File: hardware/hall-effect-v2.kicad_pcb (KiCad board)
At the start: 2 copper layers, 15 x 25 mm, 24 parts, among them P1 CON-SENSOR2, P2 DEBUG, P3 BOOT, U1 XMC1XXX24, U2 DRV023, U3 DRILL, U4 DRILL, U5 DRILL, U6 DRILL

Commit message: update sensor
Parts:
- U2: value DRV023 -> DRV5053

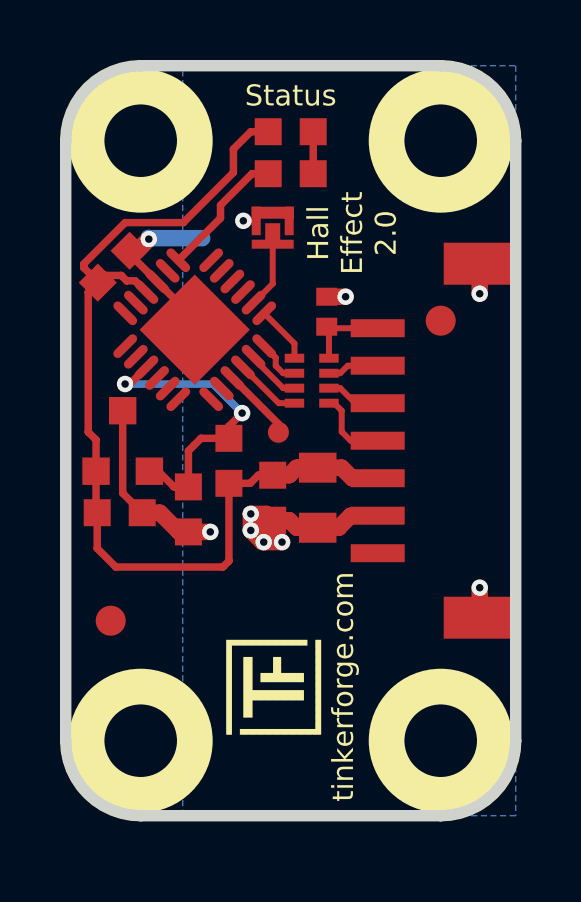
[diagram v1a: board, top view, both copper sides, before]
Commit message: add analog hall sensor with 2 reference voltages
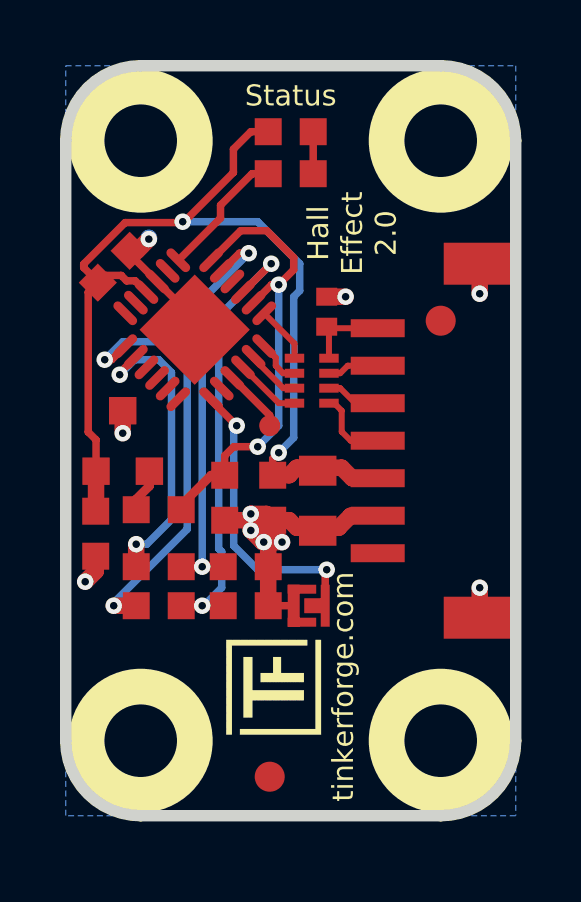
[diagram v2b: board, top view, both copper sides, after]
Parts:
- added C7: 100nF, kicad-libraries:C0603F, F.Cu at (43.9, 45.4)
- added C8: 100nF, kicad-libraries:C0603F, F.Cu at (48.2, 44.2)
- added R2: 1k, kicad-libraries:R0603F, F.Cu at (46.0, 47.8)
- added R4: 100, kicad-libraries:R0603F, F.Cu at (46.0, 44.6)
- C2: value 100nF -> 10uF; footprint kicad-libraries:C0603F -> kicad-libraries:C0805
- C3: value 10uF -> 1uF; footprint kicad-libraries:C0805 -> kicad-libraries:C0603F
- C4: value 1uF -> 100nF
- C6: value TBD -> 100nF
- P2: value DEBUG -> BOOT; footprint kicad-libraries:DEBUG_PAD -> kicad-libraries:SolderJumper
- P3: value BOOT -> DEBUG; footprint kicad-libraries:SolderJumper -> kicad-libraries:DEBUG_PAD
- R1: value TBD -> 1k
- U2: footprint SOT23-3 -> kicad-libraries:SOT23-3
- moved C5 12.1 mm to (48.9, 47.8), turned to 0 degrees
- moved C6 8.46 mm to (44.5, 36.5), turned to 45 degrees
- moved Fiducial_Mark 7.42 mm to (49.7, 53.5)
- moved C2 6.61 mm to (51.3, 44.3), turned to 270 degrees
- moved P3 6.60 mm to (49.7, 41.8)
- moved P2 5.87 mm to (51.0, 47.8)
- moved R1 4.24 mm to (46.0, 46.5), turned to 0 degrees
- moved C4 2.47 mm to (48.9, 46.5), turned to 0 degrees
- moved C3 1.50 mm to (49.8, 44.2)
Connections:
- C4 pad 1: VCC -> VOUT1
- C5 pad 1: VCC -> VOUT0
- C6 pad 1: OUT -> VCC
- P1 pad 1: Net-(P1-Pad1) -> (no net)
- P2 pad 1: Net-(P2-Pad1) -> GND
- P3 pad 1: GND -> Net-(P3-Pad1)
- R1 pad 1: OUT -> Net-(R1-Pad1)
- R1 pad 2: VCC -> VOUT1
- U1 pad 11: Net-(U1-Pad11) -> (no net)
- U1 pad 12: Net-(U1-Pad12) -> (no net)
- U1 pad 14: Net-(U1-Pad14) -> Net-(R1-Pad1)
- U1 pad 15: OUT -> (no net)
- U1 pad 16: Net-(U1-Pad16) -> (no net)
- U1 pad 17: Net-(U1-Pad17) -> (no net)
- U1 pad 18: Net-(U1-Pad18) -> (no net)
- U1 pad 19: Net-(U1-Pad19) -> Net-(P2-Pad2)
- U1 pad 2: Net-(P3-Pad2) -> OUT
- U1 pad 20: Net-(U1-Pad20) -> (no net)
- U1 pad 21: Net-(P2-Pad1) -> Net-(P3-Pad1)
- U1 pad 3: Net-(U1-Pad3) -> VOUT0
- U1 pad 4: Net-(U1-Pad4) -> (no net)
- U1 pad 5: Net-(U1-Pad5) -> VOUT1
- U1 pad 6: Net-(U1-Pad6) -> OUT
- U1 pad 8: Net-(U1-Pad8) -> (no net)
- U2 pad 2: OUT -> Net-(R4-Pad2)
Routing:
- net VOUT0: track 0.00 -> 15.2 mm, vias 0 -> 2
- net Net-(R2-Pad1): track 0.00 -> 14.1 mm, vias 0 -> 2
- net VOUT1: track 0.00 -> 13.6 mm, vias 0 -> 2
- net Net-(P2-Pad2): track 0.00 -> 10.3 mm, vias 0 -> 2
- net Net-(R1-Pad1): track 0.00 -> 10.1 mm, vias 0 -> 2
- net OUT: track 11.0 -> 15.3 mm
- net Net-(P3-Pad2): track 2.62 -> 0.00 mm
- net Net-(P2-Pad1): track 2.45 -> 0.00 mm
- net GND: track 31.0 -> 28.9 mm
- net Net-(P3-Pad1): track 0.00 -> 2.11 mm
- net VCC: track 33.0 -> 34.8 mm, vias 0 -> 2
- net Net-(R4-Pad2): track 0.00 -> 1.47 mm

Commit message: add comcu logo
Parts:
- added G***: LOGO, kicad-libraries:Logo_CoMCU, B.Cu at (50.4, 34.8)
- moved VAL 2.25 mm to (50.4, 49.8), turned to 0 degrees
- moved VAL 0.90 mm to (50.4, 42.3)
